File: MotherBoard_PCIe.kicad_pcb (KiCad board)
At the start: 2 copper layers, 91 x 196 mm, 43 parts, among them J1 XT60PB-M, J10 Bus_mechaken_PCIexpress_x16_1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, J11 Conn_01x03, J12 Conn_01x03, J13 Conn_01x03, J2 XT60PB-F, J3 Conn_01x07, J4 Conn_01x07, J5 Bus_mechaken_PCIexpress_x16_1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, J6 Bus_mechaken_PCIexpress_x16_1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, J7 Bus_mechaken_PCIexpress_x16_1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, J8 Bus_mechaken_PCIexpress_x16_1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, J9 Bus_mechaken_PCIexpress_x16_1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, U1 12V

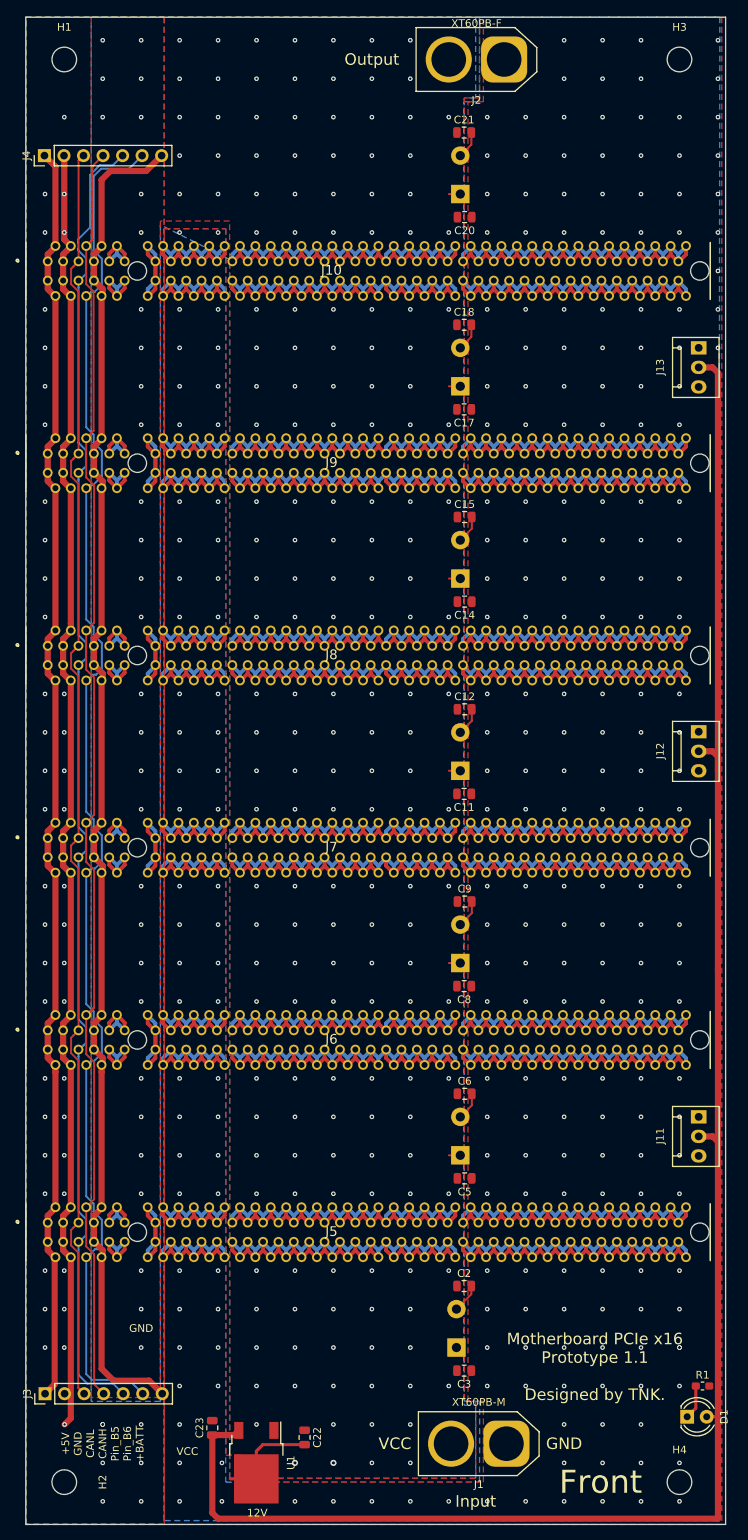
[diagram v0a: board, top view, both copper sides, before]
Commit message: change
フットプリントのリファレンスを変更したのを適応
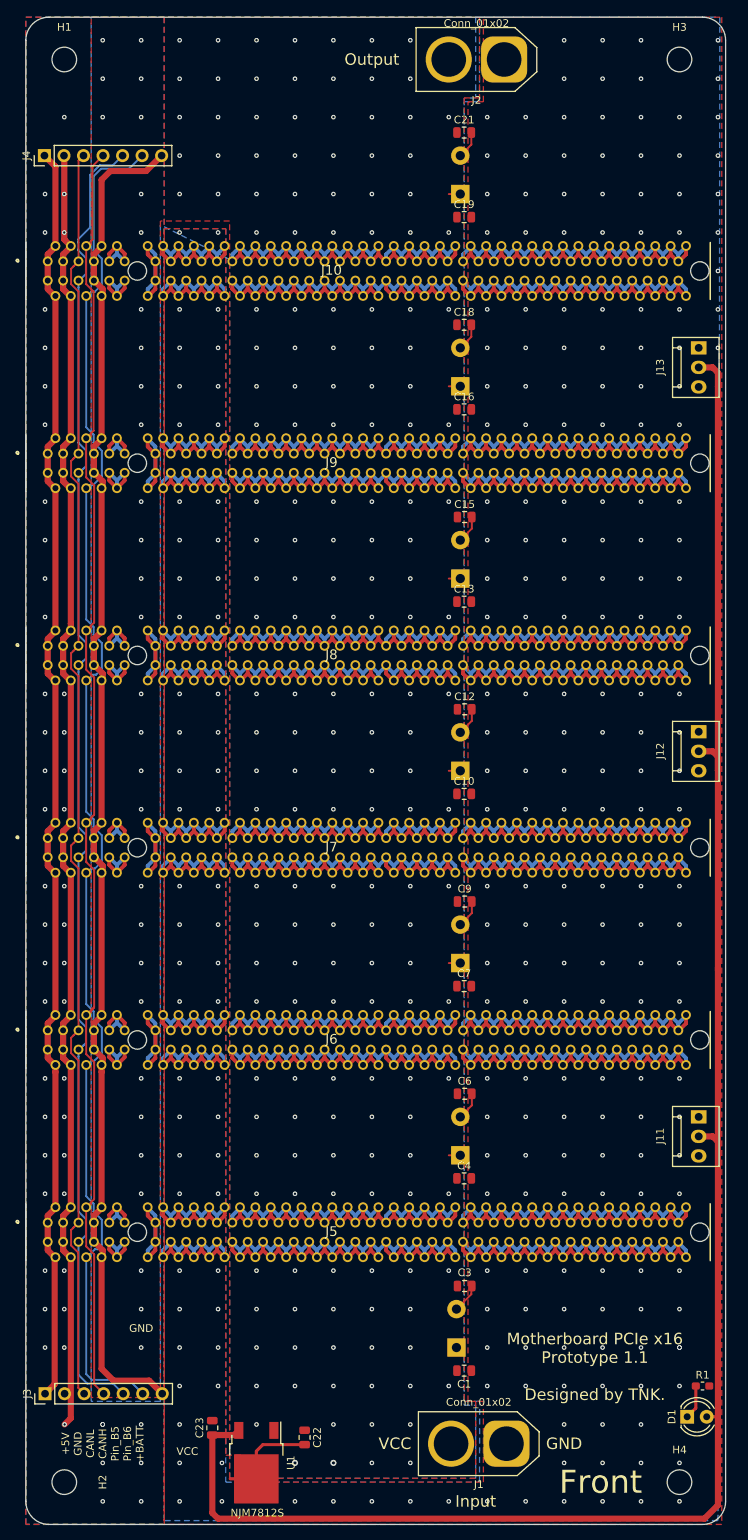
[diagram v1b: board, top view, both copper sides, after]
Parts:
- C1, C10, C13, C16, C19, C4, C7: value 1000uF -> 1u; footprint Capacitor_THT:CP_Radial_D12.5mm_P5.00mm -> Capacitor_SMD:C_0805_2012Metric; moved to F.Cu
- C11, C14, C17, C2, C20, C5, C8: value 1uF -> 1000u; footprint Capacitor_SMD:C_0805_2012Metric -> Capacitor_THT:CP_Radial_D12.5mm_P5.00mm; moved to B.Cu
- C12, C15, C18, C21, C3, C6, C9: value 10uF -> 10u
- C22: value 0.47u -> 0.33u
- J1: value XT60PB-M -> Conn_01x02
- J2: value XT60PB-F -> Conn_01x02
- U1: value 12V -> NJM7812S
- moved C3 11.0 mm to (132.1, 162.0)
- moved C2 8.06 mm to (131.0, 170.0), turned to 90 degrees
- moved C1 3.16 mm to (132.0, 173.0), turned to 0 degrees
- moved C14 3.05 mm to (131.5, 70.0), turned to 90 degrees
- moved C20 3.05 mm to (131.5, 20.0), turned to 90 degrees
- moved C5 3.05 mm to (131.5, 145.0), turned to 90 degrees
- moved C10 3.04 mm to (132.0, 98.0), turned to 0 degrees
- moved C11 3.04 mm to (131.5, 95.0), turned to 90 degrees
- moved C13 3.04 mm to (132.0, 73.0), turned to 0 degrees
- moved C16 3.04 mm to (132.0, 48.0), turned to 0 degrees
- moved C17 3.04 mm to (131.5, 45.0), turned to 90 degrees
- moved C19 3.04 mm to (132.0, 23.0), turned to 0 degrees
- moved C4 3.04 mm to (132.0, 148.0), turned to 0 degrees
- moved C7 3.04 mm to (132.0, 123.0), turned to 0 degrees
- moved C8 3.04 mm to (131.5, 120.0), turned to 90 degrees
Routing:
- net +12V: track 240.9 -> 239.9 mm
- net VCC: track 1529.7 -> 1529.1 mm
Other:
- outline, holes or cut-outs redrawn

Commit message: create
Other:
- board text added: "Motherboard PCIe x16 Prototype 1.2 Designed by TNK."
- board text removed: "Motherboard PCIe x16 Prototype 1.1 Designed by TNK."
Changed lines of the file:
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@@
     (effects (font (size 0.8 0.8) (thickness 0.12)) (justify left mirror))
   )
-  (gr_text "Motherboard PCIe x16\nPrototype 1.1\n\nDesigned by TNK." (at 149 172.5) (layer F.SilkS)
+  (gr_text "Motherboard PCIe x16\nPrototype 1.2\n\nDesigned by TNK." (at 149 172.5) (layer F.SilkS)
     (effects (font (size 1.5 1.5) (thickness 0.15)))
   )
